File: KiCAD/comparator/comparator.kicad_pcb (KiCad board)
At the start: 2 copper layers, 71.6 x 34.5 mm, 14 parts, among them J1 Output, J2 Input, U1 TLC3704, U2 TLC3704

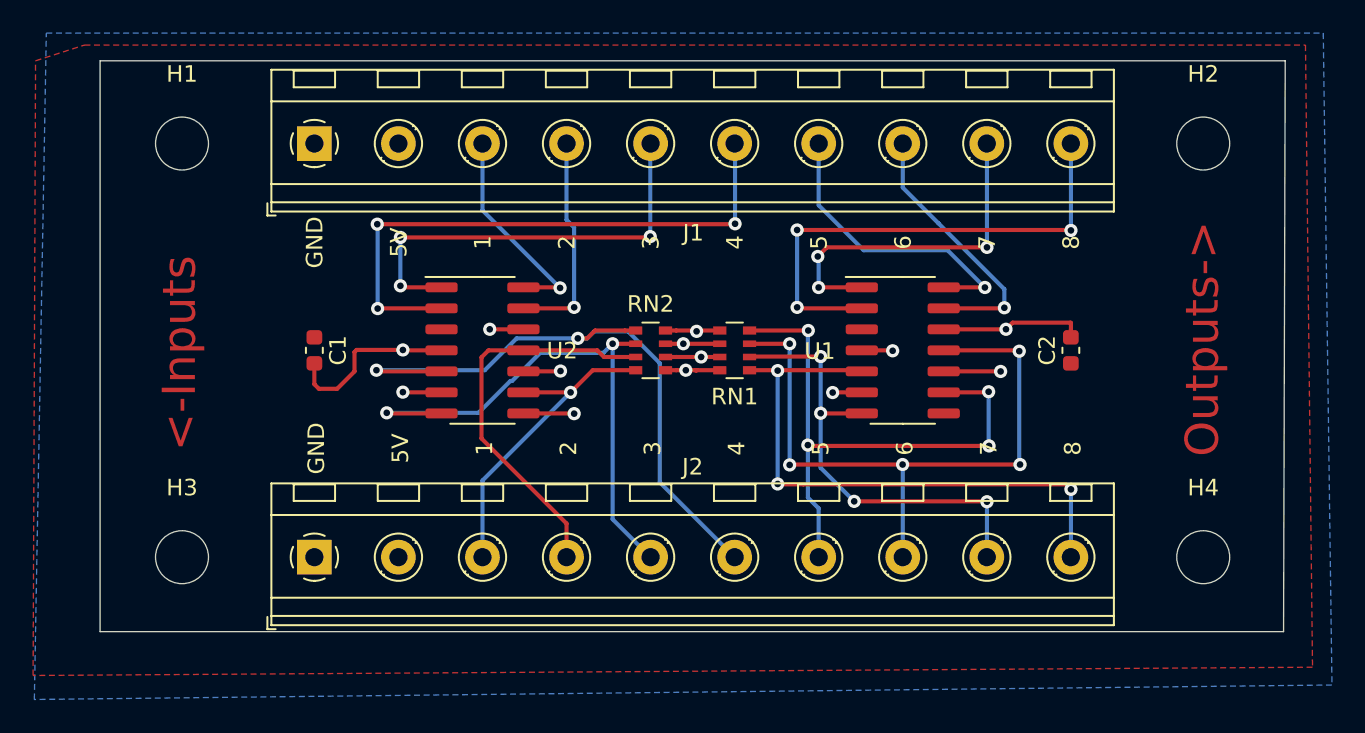
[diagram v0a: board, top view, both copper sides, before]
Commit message: added trimmer pot to the layout
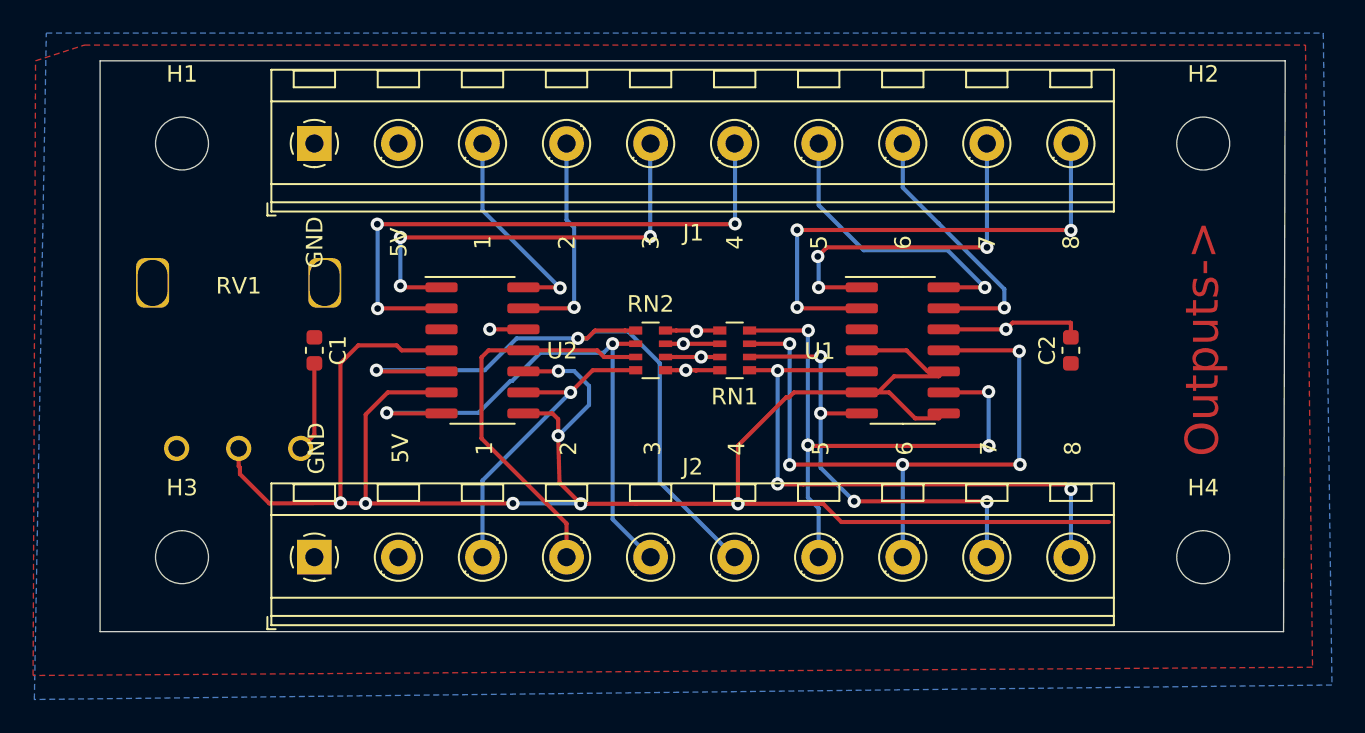
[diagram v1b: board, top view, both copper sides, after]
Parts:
- added RV1: R_POT_US, pot_TT:P120PK-Y25BR10K, F.Cu at (95.4, 108.4)
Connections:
- U1 pad 10: GNDREF -> Trimmer
- U1 pad 4: GNDREF -> Trimmer
- U1 pad 6: GNDREF -> Trimmer
- U1 pad 8: GNDREF -> Trimmer
- U2 pad 10: GNDREF -> Trimmer
- U2 pad 4: GNDREF -> Trimmer
- U2 pad 6: GNDREF -> Trimmer
- U2 pad 8: GNDREF -> Trimmer
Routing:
- net Trimmer: track 0.00 -> 126.0 mm, vias 0 -> 7
- net GNDREF: track 49.5 -> 29.5 mm, vias 13 -> 6
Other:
- board text removed: "<-Inputs"
